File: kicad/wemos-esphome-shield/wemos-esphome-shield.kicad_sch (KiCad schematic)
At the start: 13 parts, among them Q1 2N2219, T1 Transformer_1P_1S, U1 WeMos_D1_mini

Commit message: Fix some electrical net, new cut edge, new netclasses
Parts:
- added H1, H2: MountingHole, MountingHole:MountingHole_3.2mm_M3, symbol Mechanical:MountingHole
- added JP1: SolderJumper_3_Open, Jumper:SolderJumper-3_P2.0mm_Open_TrianglePad1.0x1.5mm_NumberLabels, symbol Jumper:SolderJumper_3_Open
- APDS1: value Conn_01x04_Female -> Conn_01x05_Female; symbol Connector:Conn_01x04_Female -> Connector:Conn_01x05_Female
- R1: footprint Resistor_THT:R_Axial_DIN0207_L6.3mm_D2.5mm_P15.24mm_Horizontal -> Resistor_THT:R_Axial_DIN0207_L6.3mm_D2.5mm_P10.16mm_Horizontal
- T1: symbol Device:Transformer_1P_1S -> custom:Transformer_1P_1S
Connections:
- net 3.3V: now also PIR1.2 (Pin_2), JP1.1 (A); no longer PIR1.1 (Pin_1)
- net 5V: now also APDS1.5 (Pin_5), TEMT1.3 (Pin_3), JP1.3 (B); no longer APDS1.3 (Pin_3), BME1.3 (Pin_3), TEMT1.1 (Pin_1), U1.9 (5V)
- net GND: now also BME1.2 (Pin_2), PIR1.1 (Pin_1), TEMT1.2 (Pin_2); no longer BME1.4 (Pin_4), PIR1.2 (Pin_2), TEMT1.3 (Pin_3)
- net SCL: now also APDS1.1 (Pin_1), BME1.3 (Pin_3); no longer APDS1.2 (Pin_2), BME1.2 (Pin_2)
- net SDA: now also APDS1.2 (Pin_2), BME1.4 (Pin_4); no longer APDS1.1 (Pin_1), BME1.1 (Pin_1)
- net TEMT6000: now also TEMT1.1 (Pin_1); no longer TEMT1.2 (Pin_2)
- net VCC: now also U1.9 (5V)
- new net: BME1.1 (Pin_1), JP1.2 (C)
- no-connect marks 5 -> 6
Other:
- moved on the sheet: BME1, LED1

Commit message: update APDS footprint for future compatibility
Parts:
- APDS1: footprint internal:APDS9960 -> internal:APDS9960 double pinout
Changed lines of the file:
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@@
       (effects (font (size 1.27 1.27)) (justify left))
     )
-    (property "Footprint" "internal:APDS9960" (id 2) (at 179.07 58.42 0)
+    (property "Footprint" "internal:APDS9960 double pinout" (id 2) (at 179.07 58.42 0)
       (effects (font (size 1.27 1.27)) hide)
     )
@@
   (symbol_instances
     (path "/3fcd1565-3fed-48e7-a513-b35879eb331c"
-      (reference "APDS1") (unit 1) (value "Conn_01x05_Female") (footprint "internal:APDS9960")
+      (reference "APDS1") (unit 1) (value "Conn_01x05_Female") (footprint "internal:APDS9960 double pinout")
     )
     (path "/4aa4f53a-1c9a-4e3e-a306-aaddf84769e0"

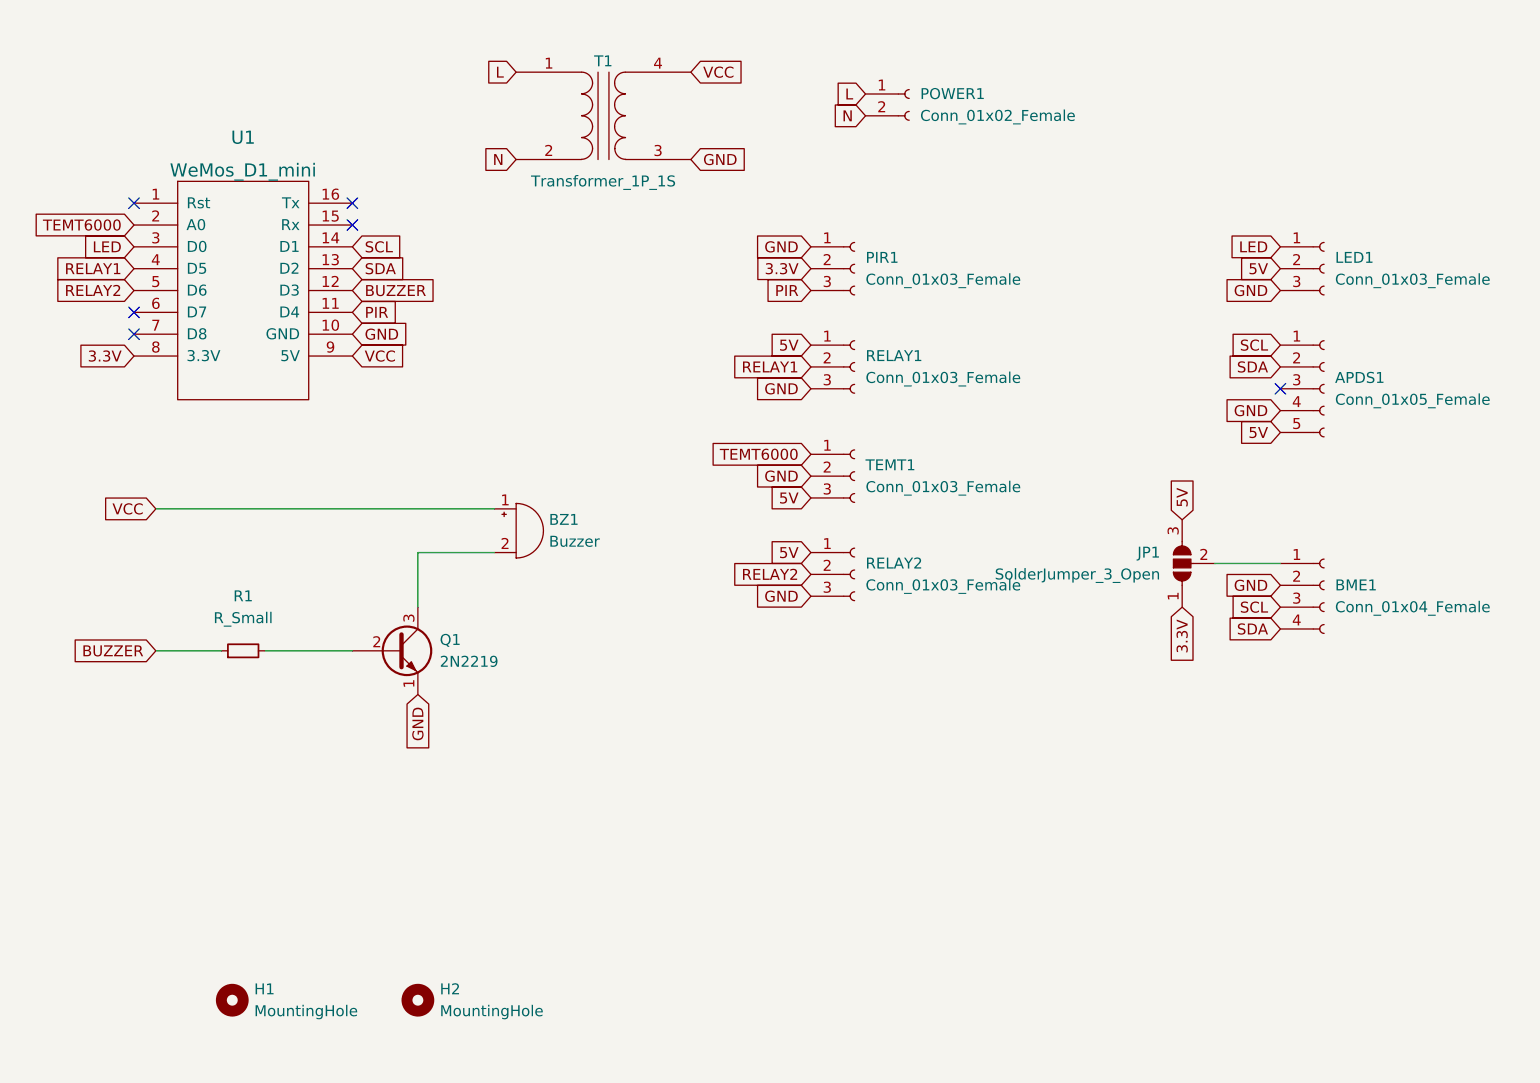
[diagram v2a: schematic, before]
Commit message: transistor driven relay pin, expose more extra pins, and routing
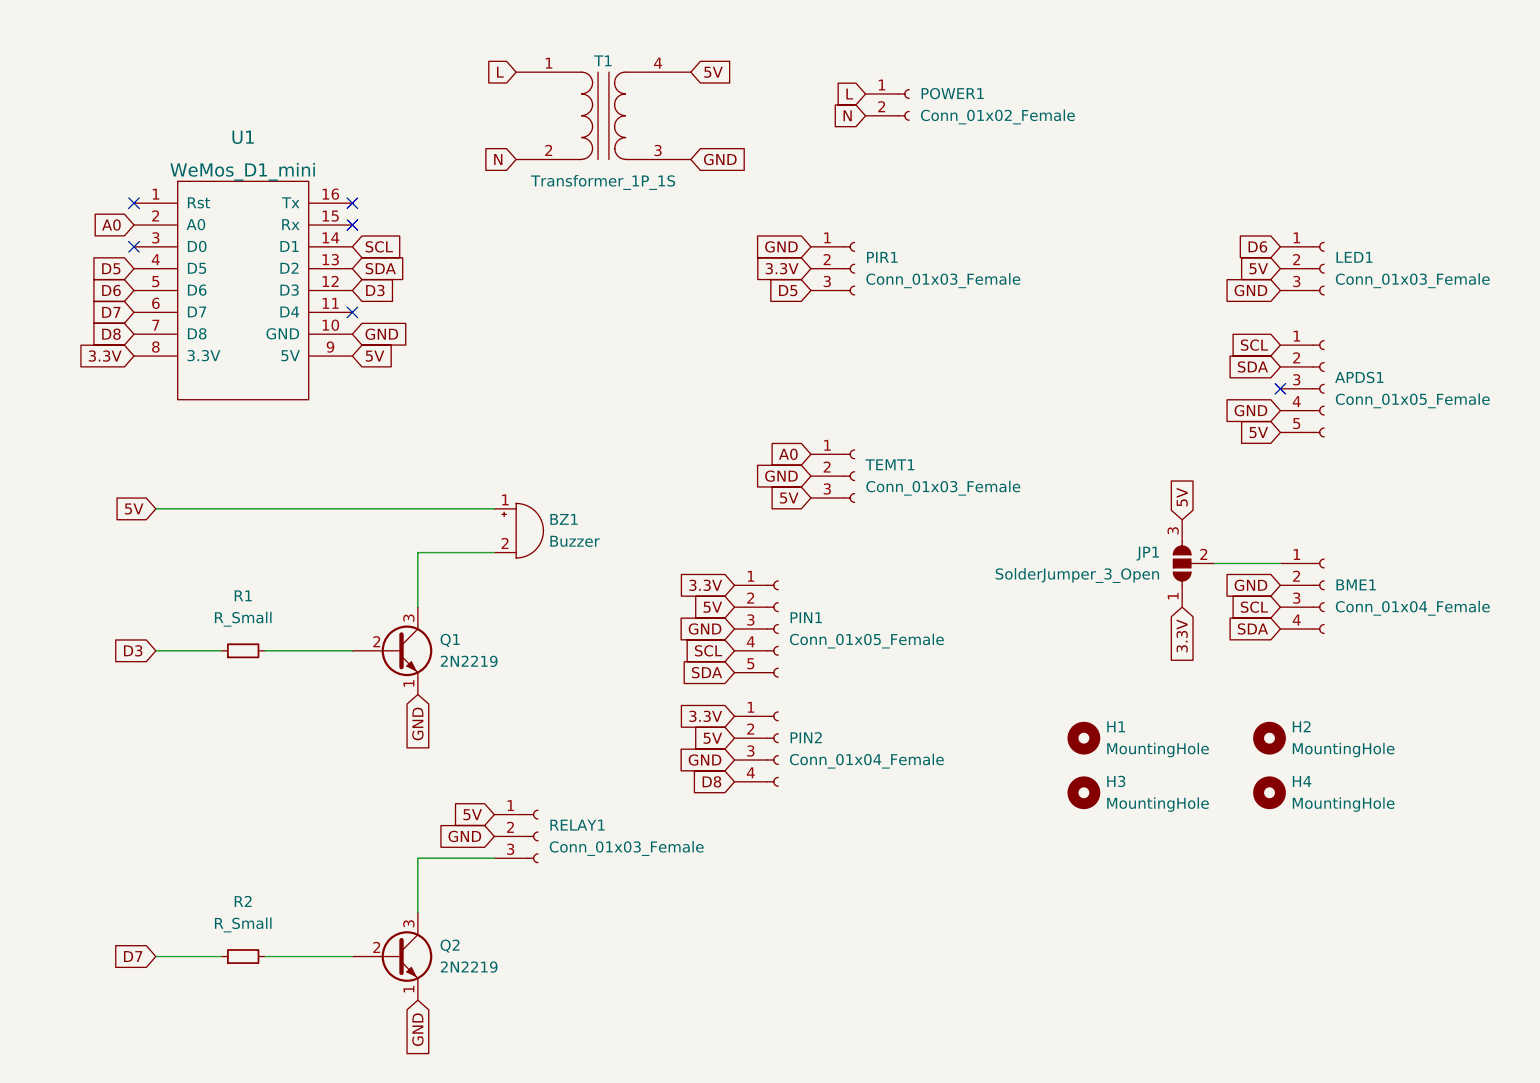
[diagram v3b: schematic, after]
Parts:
- removed RELAY2: Conn_01x03_Female, Connector_PinHeader_2.54mm:PinHeader_1x03_P2.54mm_Vertical, symbol Connector:Conn_01x03_Female
- added H3, H4: MountingHole, MountingHole:MountingHole_3.2mm_M3, symbol Mechanical:MountingHole
- added PIN1: Conn_01x05_Female, Connector_PinHeader_2.54mm:PinHeader_1x05_P2.54mm_Vertical, symbol Connector:Conn_01x05_Female
- added PIN2: Conn_01x04_Female, Connector_PinHeader_2.54mm:PinHeader_1x04_P2.54mm_Vertical, symbol Connector:Conn_01x04_Female
- added Q2: 2N2219, Package_TO_SOT_THT:TO-92L_Inline, symbol Transistor_BJT:2N2219
- added R2: R_Small, Resistor_THT:R_Axial_DIN0207_L6.3mm_D2.5mm_P10.16mm_Horizontal, symbol Device:R_Small
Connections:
- net VCC is gone; now on net 5V: BZ1.1 (-), T1.4 (SB), U1.9 (5V)
- net 3.3V: now also PIN1.1 (Pin_1), PIN2.1 (Pin_1)
- net 5V: now also PIN1.2 (Pin_2), PIN2.2 (Pin_2)
- net GND: now also RELAY1.2 (Pin_2), PIN1.3 (Pin_3), PIN2.3 (Pin_3), Q2.1 (E); no longer RELAY1.3 (Pin_3)
- net SCL: now also PIN1.4 (Pin_4)
- net SDA: now also PIN1.5 (Pin_5)
- net D7: now reaches U1.6 (D7)
- net D7: now also R2.1
- net D8: now reaches U1.7 (D8)
- net D8: now also PIN2.4 (Pin_4)
- net BUZZER renamed D3
- net LED: no longer names the net of U1.3 (D0)
- net LED: no longer LED1.1 (Pin_1)
- net PIR: no longer names the net of U1.11 (D4)
- net PIR: no longer PIR1.3 (Pin_3)
- net RELAY1 renamed D5
- net D5: now also PIR1.3 (Pin_3); no longer RELAY1.2 (Pin_2)
- net RELAY2 renamed D6
- net D6: now also LED1.1 (Pin_1)
- net TEMT6000 renamed A0
- new net: Q2.2 (B), R2.2
- new net: Q2.3 (C), RELAY1.3 (Pin_3)
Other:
- moved on the sheet: H1, H2, RELAY1

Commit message: add oled screen pads
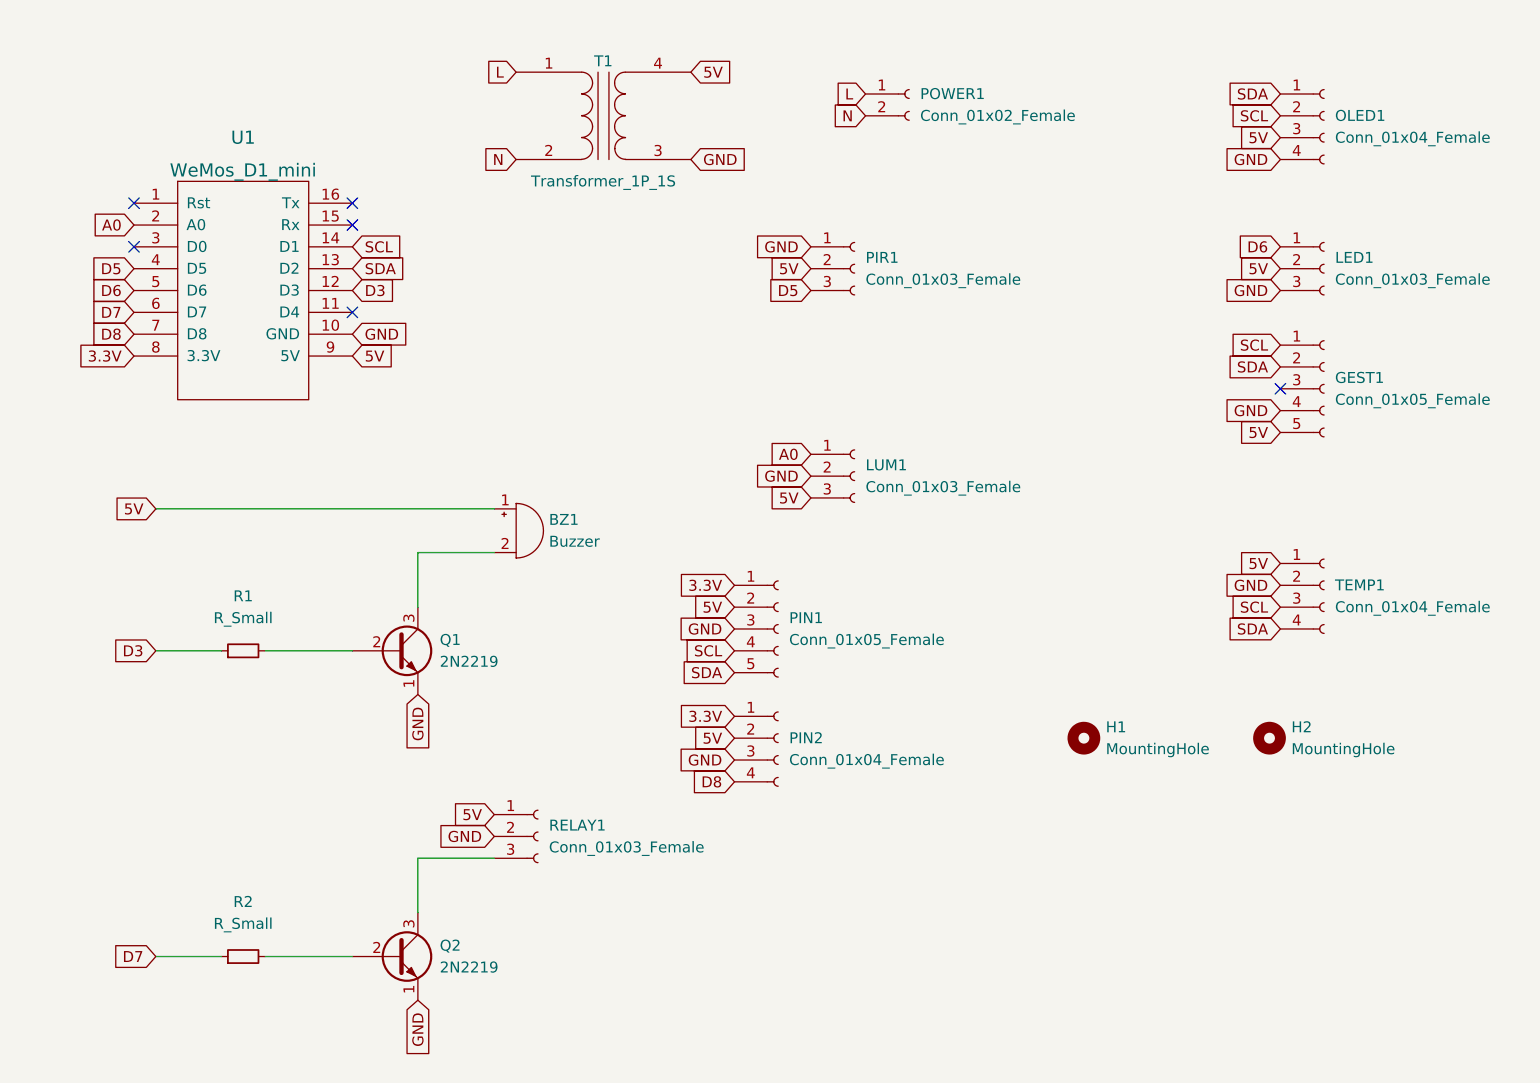
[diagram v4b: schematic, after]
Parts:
- removed H3, H4: MountingHole, MountingHole:MountingHole_3.2mm_M3, symbol Mechanical:MountingHole
- removed JP1: SolderJumper_3_Open, Jumper:SolderJumper-3_P2.0mm_Open_TrianglePad1.0x1.5mm_NumberLabels, symbol Jumper:SolderJumper_3_Open
- added OLED1: Conn_01x04_Female, internal:SSD1306 OLED 128x32, symbol Connector:Conn_01x04_Female
- renumbered APDS1 to GEST1, TEMT1 to LUM1, BME1 to TEMP1
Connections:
- net 3.3V: no longer PIR1.2 (Pin_2)
- net 5V: now also PIR1.2 (Pin_2), TEMP1.1 (Pin_1), OLED1.3 (Pin_3)
- net GND: now also OLED1.4 (Pin_4)
- net SCL: now also OLED1.2 (Pin_2)
- net SDA: now also OLED1.1 (Pin_1)

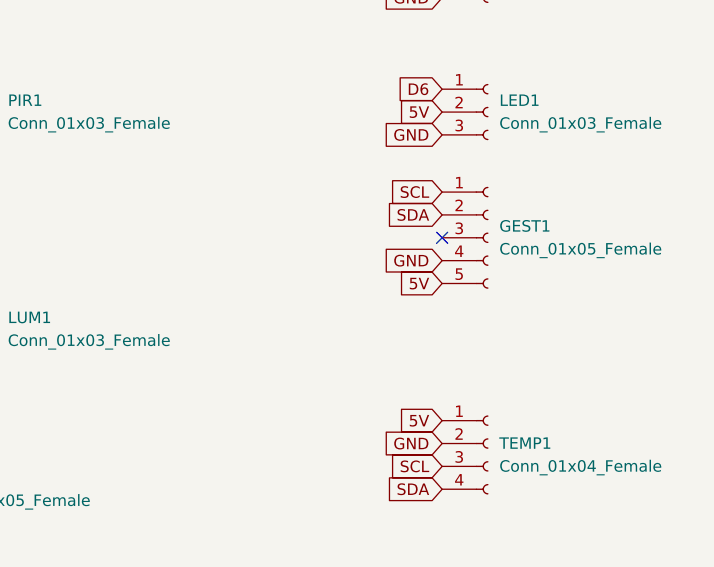
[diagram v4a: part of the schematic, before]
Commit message: fix schema and routing for APDS9960
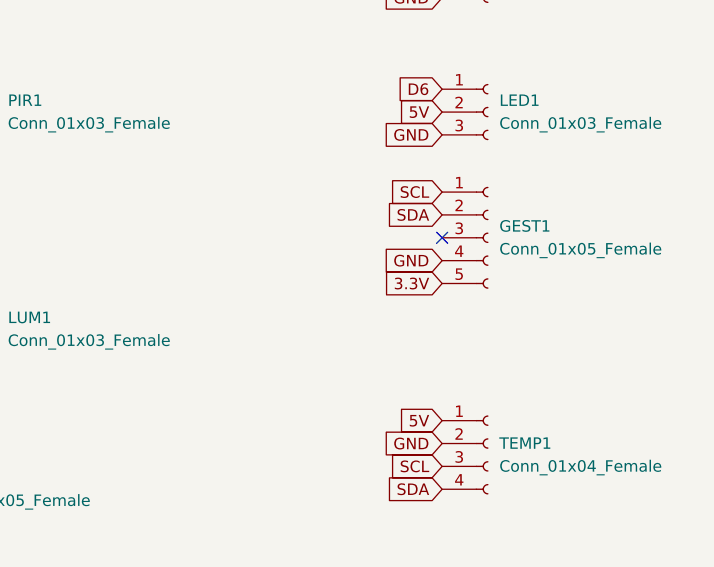
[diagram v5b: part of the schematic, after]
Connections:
- net 3.3V: now also GEST1.5 (Pin_5)
- net 5V: no longer GEST1.5 (Pin_5)
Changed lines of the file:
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@@
+    )
+  )
+  (global_label "3.3V" (shape input) (at 173.99 63.5 180) (fields_autoplaced)
+    (effects (font (size 1.27 1.27)) (justify right))
+    (property "Intersheet References" "${INTERSHEET_REFS}" (id 0) (at 167.4645 63.4206 0)
+      (effects (font (size 1.27 1.27)) (justify right) hide)
     )
   )
@@
       (effects (font (size 1.27 1.27)) (justify right) hide)
     )
-  )
-  (global_label "5V" (shape input) (at 173.99 63.5 180) (fields_autoplaced)
-    (effects (font (size 1.27 1.27)) (justify right))
-    (property "Intersheet References" "${INTERSHEET_REFS}" (id 0) (at 169.2788 63.4206 0)
-      (effects (font (size 1.27 1.27)) (justify right) hide)
-    )

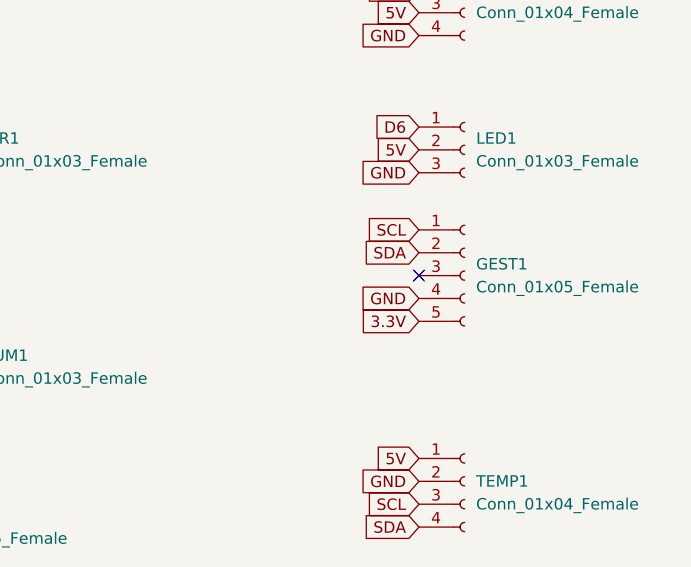
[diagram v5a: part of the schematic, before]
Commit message: fix schema and routing for apds9960
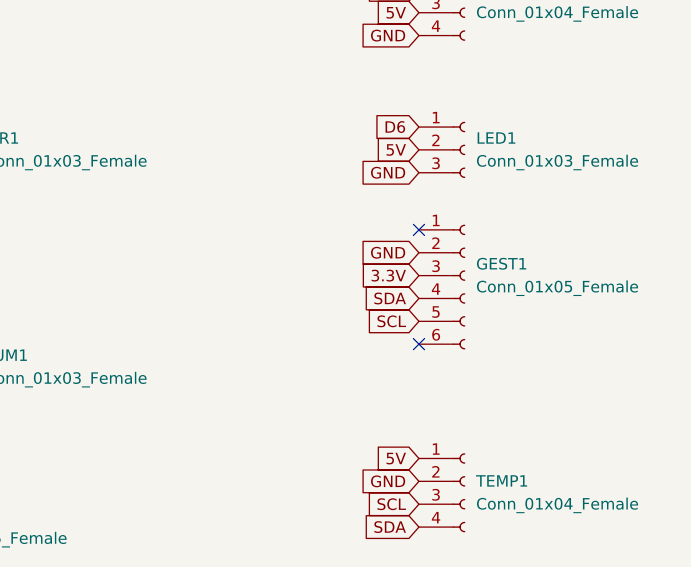
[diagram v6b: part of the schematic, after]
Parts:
- GEST1: footprint internal:APDS9960 double pinout -> internal:APDS9960; symbol Connector:Conn_01x05_Female -> Connector:Conn_01x06_Female
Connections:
- net 3.3V: now also GEST1.3 (Pin_3); no longer GEST1.5 (Pin_5)
- net GND: now also GEST1.2 (Pin_2); no longer GEST1.4 (Pin_4)
- net SCL: now also GEST1.5 (Pin_5); no longer GEST1.1 (Pin_1)
- net SDA: now also GEST1.4 (Pin_4); no longer GEST1.2 (Pin_2)
- no-connect marks 6 -> 7
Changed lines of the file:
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@@
   (no_connect (at 66.04 36.83))
   (no_connect (at 40.64 41.91))
-  (no_connect (at 173.99 58.42))
+  (no_connect (at 173.99 53.34))
+  (no_connect (at 173.99 66.04))
   (wire (pts (xy 55.88 88.9) (xy 66.04 88.9))
     (stroke (width 0) (type default) (color 0 0 0 0))
@@
     )
   )
-  (global_label "3.3V" (shape input) (at 173.99 63.5 180) (fields_autoplaced)
-    (effects (font (size 1.27 1.27)) (justify right))
-    (property "Intersheet References" "${INTERSHEET_REFS}" (id 0) (at 167.4645 63.4206 0)
+  (global_label "3.3V" (shape input) (at 173.99 58.42 180) (fields_autoplaced)
+    (effects (font (size 1.27 1.27)) (justify right))
+    (property "Intersheet References" "${INTERSHEET_REFS}" (id 0) (at 167.4645 58.3406 0)
       (effects (font (size 1.27 1.27)) (justify right) hide)
     )
@@
     )
   )
-  (global_label "GND" (shape input) (at 173.99 60.96 180) (fields_autoplaced)
-    (effects (font (size 1.27 1.27)) (justify right))
-    (property "Intersheet References" "${INTERSHEET_REFS}" (id 0) (at 167.7064 60.8806 0)
+  (global_label "GND" (shape input) (at 173.99 55.88 180) (fields_autoplaced)
+    (effects (font (size 1.27 1.27)) (justify right))
+    (property "Intersheet References" "${INTERSHEET_REFS}" (id 0) (at 167.7064 55.8006 0)
       (effects (font (size 1.27 1.27)) (justify right) hide)
     )
@@
     )
   )
-  (global_label "SCL" (shape input) (at 173.99 53.34 180) (fields_autoplaced)
-    (effects (font (size 1.27 1.27)) (justify right))
-    (property "Intersheet References" "${INTERSHEET_REFS}" (id 0) (at 168.0693 53.4194 0)
+  (global_label "SCL" (shape input) (at 173.99 63.5 180) (fields_autoplaced)
+    (effects (font (size 1.27 1.27)) (justify right))
+    (property "Intersheet References" "${INTERSHEET_REFS}" (id 0) (at 168.0693 63.5794 0)
       (effects (font (size 1.27 1.27)) (justify right) hide)
     )
@@
     )
   )
-  (global_label "SDA" (shape input) (at 173.99 55.88 180) (fields_autoplaced)
-    (effects (font (size 1.27 1.27)) (justify right))
-    (property "Intersheet References" "${INTERSHEET_REFS}" (id 0) (at 168.0088 55.9594 0)
+  (global_label "SDA" (shape input) (at 173.99 60.96 180) (fields_autoplaced)
+    (effects (font (size 1.27 1.27)) (justify right))
+    (property "Intersheet References" "${INTERSHEET_REFS}" (id 0) (at 168.0088 61.0394 0)
       (effects (font (size 1.27 1.27)) (justify right) hide)
     )
@@
     (pin "3")
   )
-  (symbol (lib_id "Connector:Conn_01x05_Female") (at 179.07 58.42 0) (unit 1)
+  (symbol (lib_id "Connector:Conn_01x06_Female") (at 179.07 58.42 0) (unit 1)
     (in_bom yes) (on_board yes) (fields_autoplaced)
     (property "Reference" "GEST1" (id 0) (at 180.34 57.1499 0)
@@
       (effects (font (size 1.27 1.27)) (justify left))
     )
-    (property "Footprint" "internal:APDS9960 double pinout" (id 2) (at 179.07 58.42 0)
+    (property "Footprint" "internal:APDS9960" (id 2) (at 179.07 58.42 0)
       (effects (font (size 1.27 1.27)) hide)
     )
@@
     (pin "4")
     (pin "5")
+    (pin "6")
   )
   (symbol (lib_id "Connector:Conn_01x04_Female") (at 179.07 81.28 0) (unit 1)
@@
     )
     (path "/3fcd1565-3fed-48e7-a513-b35879eb331c"
-      (reference "GEST1") (unit 1) (value "Conn_01x05_Female") (footprint "internal:APDS9960 double pinout")
+      (reference "GEST1") (unit 1) (value "Conn_01x05_Female") (footprint "internal:APDS9960")
     )
     (path "/55b1e705-376b-4963-89b4-8ab5ad7669cb"
